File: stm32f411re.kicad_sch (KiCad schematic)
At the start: 32 parts, among them J1 ADC, J2 USB_OTG, J3 SD, J4 SPI, J5 UART, J6 I2C, J7 GPIO_Digital_I/O, J8 GPIO_Analog_pins, SW1 BOOT_SW, SW2 Reset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

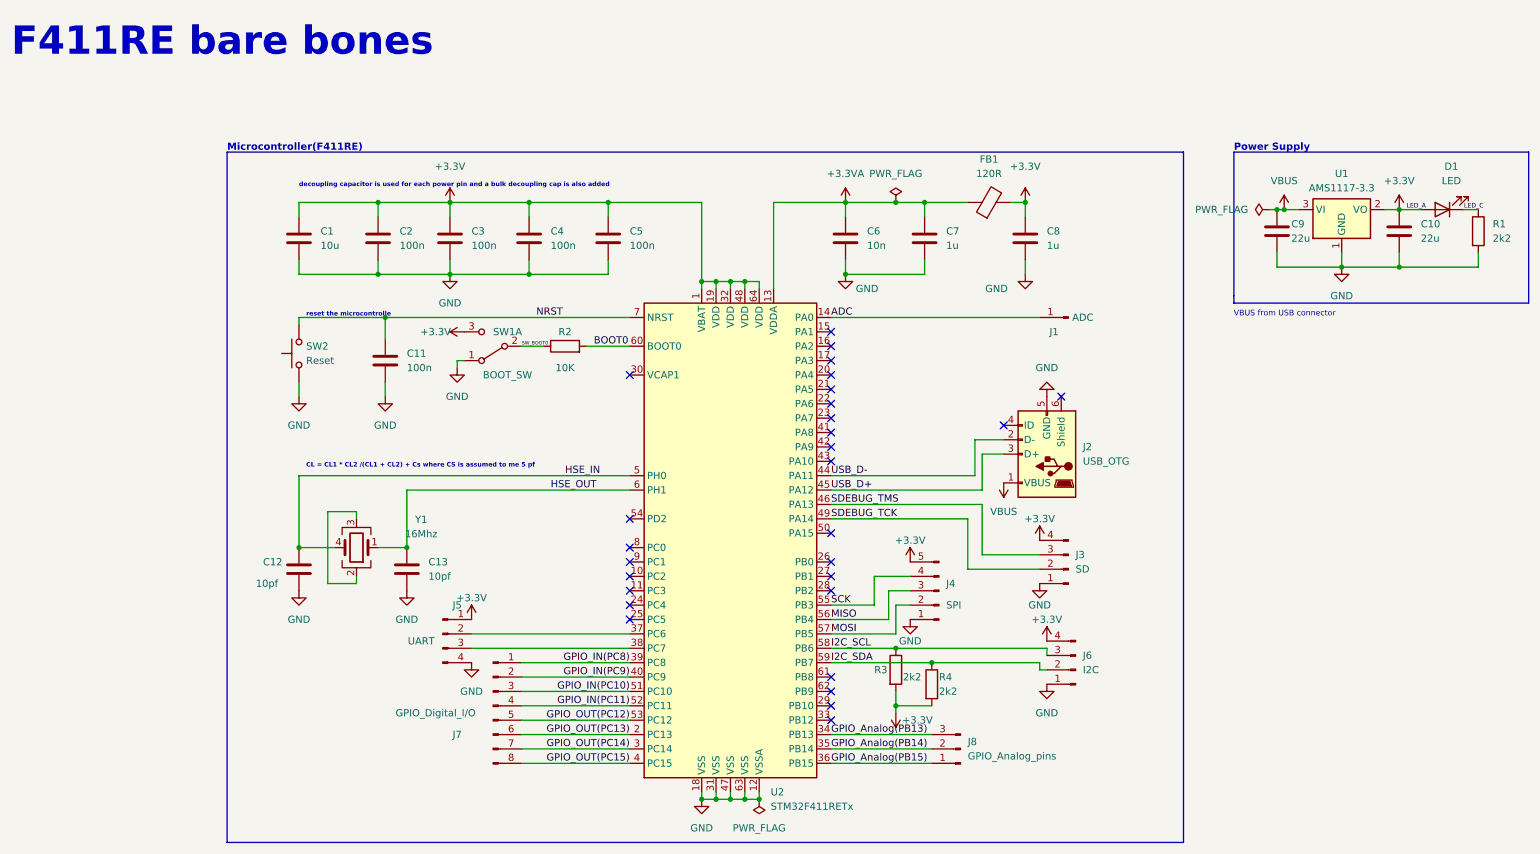
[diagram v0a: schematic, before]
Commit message: changed some footprints in the schemaitcs and also done some PCB layout for the board
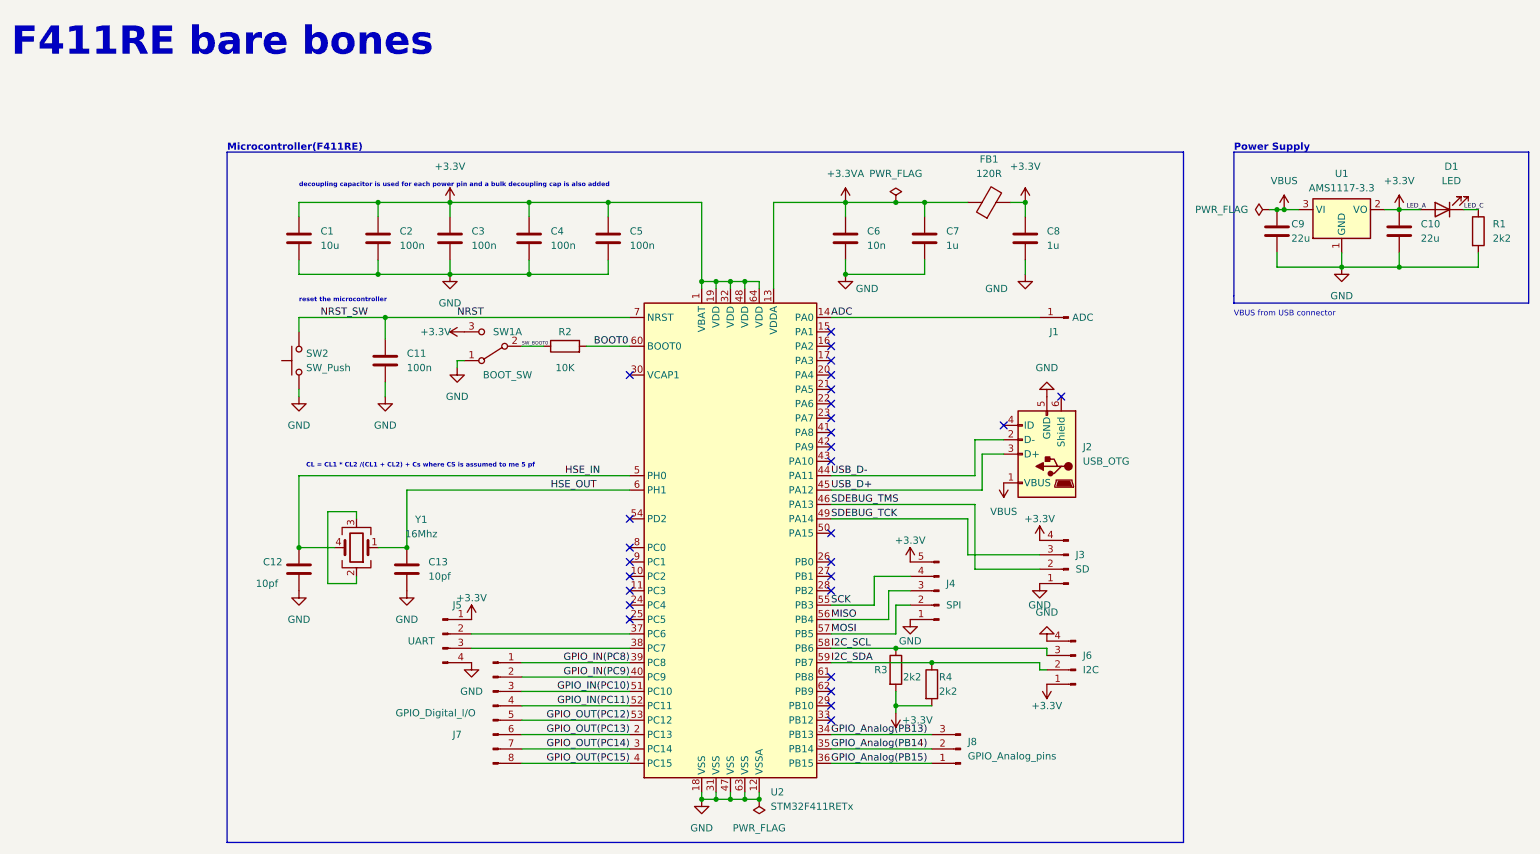
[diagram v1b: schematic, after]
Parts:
- removed SW2: Reset, Button_Switch_SMD:SW_MEC_5GSH9, symbol Switch:SW_MEC_5G
- added SW2: SW_Push, Button_Switch_SMD:SW_SPST_B3U-1000P-B, symbol Switch:SW_Push
- SW1: footprint Button_Switch_THT:SW_CuK_JS202011CQN_DPDT_Straight -> Button_Switch_SMD:SW_SPDT_PCM12
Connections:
- net +3.3V: now also J6.1 (Pin_1); no longer J6.4 (Pin_4)
- net GND: now also J6.4 (Pin_4), SW2.1; no longer J6.1 (Pin_1)
- net NRST: now also SW2.2
- net SDEBUG_TCK: now also J3.3 (Pin_3); no longer J3.2 (Pin_2)
- net SDEBUG_TMS: now also J3.2 (Pin_2); no longer J3.3 (Pin_3)
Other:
- note added: "reset the microcontroller"
- note removed: "reset the microcontrolle"

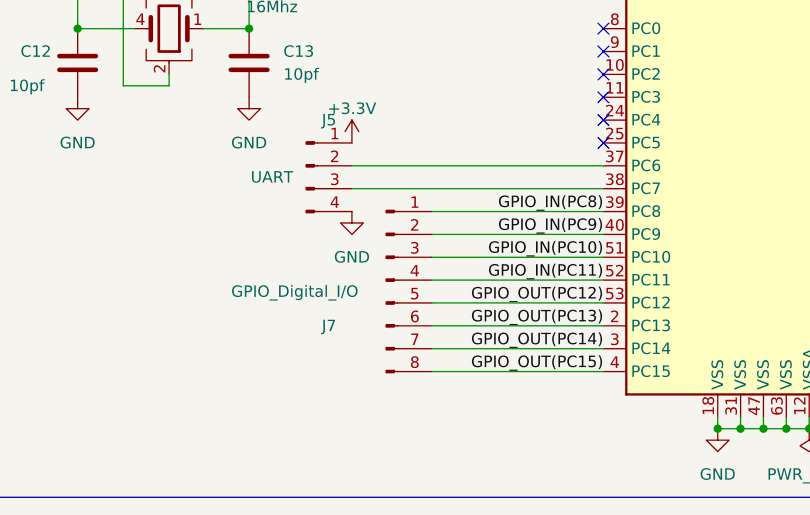
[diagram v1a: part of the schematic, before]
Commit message: removed the GPIO input and outpins (want to redo them) and mostly finished the first pcb layout
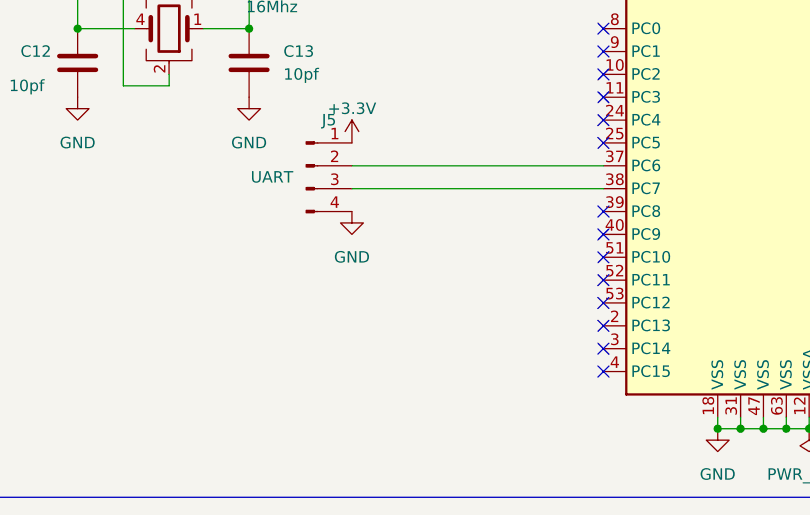
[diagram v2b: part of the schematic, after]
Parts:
- removed J7: GPIO_Digital_I/O, Connector_PinHeader_2.54mm:PinHeader_1x08_P2.54mm_Vertical, symbol Connector:Conn_01x08_Pin
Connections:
- net GPIO_IN(PC10): no longer names the net of U2.51 (PC10)
- net GPIO_IN(PC11): no longer names the net of U2.52 (PC11)
- net GPIO_IN(PC8): no longer names the net of U2.39 (PC8)
- net GPIO_IN(PC9): no longer names the net of U2.40 (PC9)
- net GPIO_OUT(PC12): no longer names the net of U2.53 (PC12)
- net GPIO_OUT(PC13): no longer names the net of U2.2 (PC13)
- net GPIO_OUT(PC14): no longer names the net of U2.3 (PC14)
- net GPIO_OUT(PC15): no longer names the net of U2.4 (PC15)
- no-connect marks 28 -> 36
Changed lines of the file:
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@@
   )
   (no_connect (at 125.73 114.3))
+  (no_connect (at 125.73 129.54))
   (no_connect (at 161.29 111.76))
   (no_connect (at 191.77 87.63))
   (no_connect (at 125.73 78.74))
+  (no_connect (at 125.73 147.32))
+  (no_connect (at 125.73 144.78))
   (no_connect (at 161.29 114.3))
   (no_connect (at 161.29 76.2))
   (no_connect (at 125.73 109.22))
   (no_connect (at 161.29 81.28))
+  (no_connect (at 125.73 132.08))
   (no_connect (at 161.29 93.98))
   (no_connect (at 161.29 78.74))
   (no_connect (at 161.29 139.7))
+  (no_connect (at 125.73 142.24))
   (no_connect (at 125.73 119.38))
   (no_connect (at 161.29 83.82))
+  (no_connect (at 125.73 139.7))
   (no_connect (at 125.73 116.84))
   (no_connect (at 161.29 71.12))
@@
   (no_connect (at 161.29 106.68))
   (no_connect (at 161.29 88.9))
+  (no_connect (at 125.73 134.62))
   (no_connect (at 161.29 116.84))
   (no_connect (at 161.29 137.16))
   (no_connect (at 125.73 111.76))
+  (no_connect (at 125.73 137.16))
   (no_connect (at 161.29 132.08))
   (no_connect (at 125.73 121.92))
@@
     (stroke (width 0) (type default))
   )
-  (wire (pts (xy 106.68 139.7) (xy 125.73 139.7))
-    (stroke (width 0) (type default))
-  )
   (wire (pts (xy 177.8 48.26) (xy 185.42 48.26))
     (stroke (width 0) (type default))
@@
     (stroke (width 0) (type default))
   )
-  (wire (pts (xy 106.68 147.32) (xy 125.73 147.32))
-    (stroke (width 0) (type default))
-  )
   (wire (pts (xy 241.3 49.53) (xy 243.84 49.53))
     (stroke (width 0) (type default))
@@
     (stroke (width 0) (type default))
   )
-  (wire (pts (xy 106.68 144.78) (xy 125.73 144.78))
-    (stroke (width 0) (type default))
-  )
   (wire (pts (xy 107.95 48.26) (xy 107.95 50.8))
     (stroke (width 0) (type default))
   )
-  (wire (pts (xy 106.68 132.08) (xy 125.73 132.08))
-    (stroke (width 0) (type default))
-  )
   (wire (pts (xy 163.83 58.42) (xy 163.83 60.96))
     (stroke (width 0) (type default))
@@
     (stroke (width 0) (type default))
   )
-  (wire (pts (xy 106.68 129.54) (xy 125.73 129.54))
-    (stroke (width 0) (type default))
-  )
   (wire (pts (xy 143.51 153.67) (xy 146.05 153.67))
     (stroke (width 0) (type default))
@@
     (stroke (width 0) (type default))
   )
-  (wire (pts (xy 106.68 137.16) (xy 125.73 137.16))
-    (stroke (width 0) (type default))
-  )
   (wire (pts (xy 81.28 60.96) (xy 93.98 60.96))
     (stroke (width 0) (type default))
@@
     (stroke (width 0) (type default))
   )
-  (wire (pts (xy 106.68 134.62) (xy 125.73 134.62))
-    (stroke (width 0) (type default))
-  )
   (wire (pts (xy 77.47 102.87) (xy 77.47 104.14))
     (stroke (width 0) (type default))
@@
   )
   (wire (pts (xy 140.97 62.23) (xy 138.43 62.23))
-    (stroke (width 0) (type default))
-  )
-  (wire (pts (xy 106.68 142.24) (xy 125.73 142.24))
     (stroke (width 0) (type default))
   )
@@
     (effects (font (size 1.27 1.27)) (justify left bottom))
   )
-  (label "GPIO_IN(PC10)" (at 125.73 134.62 180) (fields_autoplaced)
-    (effects (font (size 1.27 1.27)) (justify right bottom))
-  )
-  (label "GPIO_IN(PC8)" (at 125.73 129.54 180) (fields_autoplaced)
-    (effects (font (size 1.27 1.27)) (justify right bottom))
-  )
   (label "LED_C" (at 273.05 49.53 0) (fields_autoplaced)
     (effects (font (size 0.8 0.8)) (justify left bottom))
@@
     (effects (font (size 1.27 1.27)) (justify left bottom))
   )
-  (label "GPIO_IN(PC9)" (at 125.73 132.08 180) (fields_autoplaced)
-    (effects (font (size 1.27 1.27)) (justify right bottom))
-  )
   (label "MOSI" (at 161.29 124.46 0) (fields_autoplaced)
     (effects (font (size 1.27 1.27)) (justify left bottom))
@@
     (effects (font (size 1.27 1.27)) (justify left bottom))
   )
-  (label "GPIO_OUT(PC14)" (at 125.73 144.78 180) (fields_autoplaced)
-    (effects (font (size 1.27 1.27)) (justify right bottom))
-  )
   (label "USB_D+" (at 161.29 99.06 0) (fields_autoplaced)
     (effects (font (size 1.27 1.27)) (justify left bottom))
-  )
-  (label "GPIO_OUT(PC15)" (at 125.73 147.32 180) (fields_autoplaced)
-    (effects (font (size 1.27 1.27)) (justify right bottom))
   )
   (label "LED_A" (at 262.89 49.53 0) (fields_autoplaced)
@@
     (effects (font (size 1.27 1.27)) (justify left bottom))
   )
-  (label "GPIO_OUT(PC12)" (at 125.73 139.7 180) (fields_autoplaced)
-    (effects (font (size 1.27 1.27)) (justify right bottom))
-  )
-  (label "GPIO_OUT(PC13)" (at 125.73 142.24 180) (fields_autoplaced)
-    (effects (font (size 1.27 1.27)) (justify right bottom))
-  )
   (label "MISO" (at 161.29 121.92 0) (fields_autoplaced)
     (effects (font (size 1.27 1.27)) (justify left bottom))
@@
   (label "GPIO_Analog(PB15)" (at 161.29 147.32 0) (fields_autoplaced)
     (effects (font (size 1.27 1.27)) (justify left bottom))
-  )
-  (label "GPIO_IN(PC11)" (at 125.73 137.16 180) (fields_autoplaced)
-    (effects (font (size 1.27 1.27)) (justify right bottom))
   )
   (label "SDEBUG_TMS" (at 161.29 101.6 0) (fields_autoplaced)
@@
         )
       )
-    )
-  )
-  (symbol (lib_id "Connector:Conn_01x08_Pin") (at 101.6 137.16 0) (unit 1)
-    (in_bom yes) (on_board yes) (dnp no)
-    (property "Reference" "J7" (at 95.25 142.24 0)
-      (effects (font (size 1.27 1.27)))
-    )
-    (property "Value" "GPIO_Digital_I/O" (at 91.44 138.43 0)
-      (effects (font (size 1.27 1.27)))
-    )
-    (property "Footprint" "Connector_PinHeader_2.54mm:PinHeader_1x08_P2.54mm_Vertical" (at 101.6 137.16 0)
-      (effects (font (size 1.27 1.27)) hide)
-    )
-    (property "Datasheet" "~" (at 101.6 137.16 0)
-      (effects (font (size 1.27 1.27)) hide)
-    )
-    (pin "1")
-    (pin "2")
-    (pin "3")
-    (pin "4")
-    (pin "5")
-    (pin "6")
-    (pin "7")
-    (pin "8")
-    (instances
-      (project "stm32f411re"
-        (path "/cf983ff0-805d-4746-8911-be6db2d7861c"
-          (reference "J7") (unit 1)
-        )
-      )
